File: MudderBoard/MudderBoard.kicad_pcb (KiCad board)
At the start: 2 copper layers, 157 parts, among them K1 AZ2850-2A-12DE, M1 NMOS, M2 NMOS, M3 N-MOSFET, M4 N-MOSFET, Q1 CSD16327Q3, Q2 NPN, U1 LM5122QMH/NOPB, U2 TPS566242DRLR, U3 LP38691DTX-3.3/NOPB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

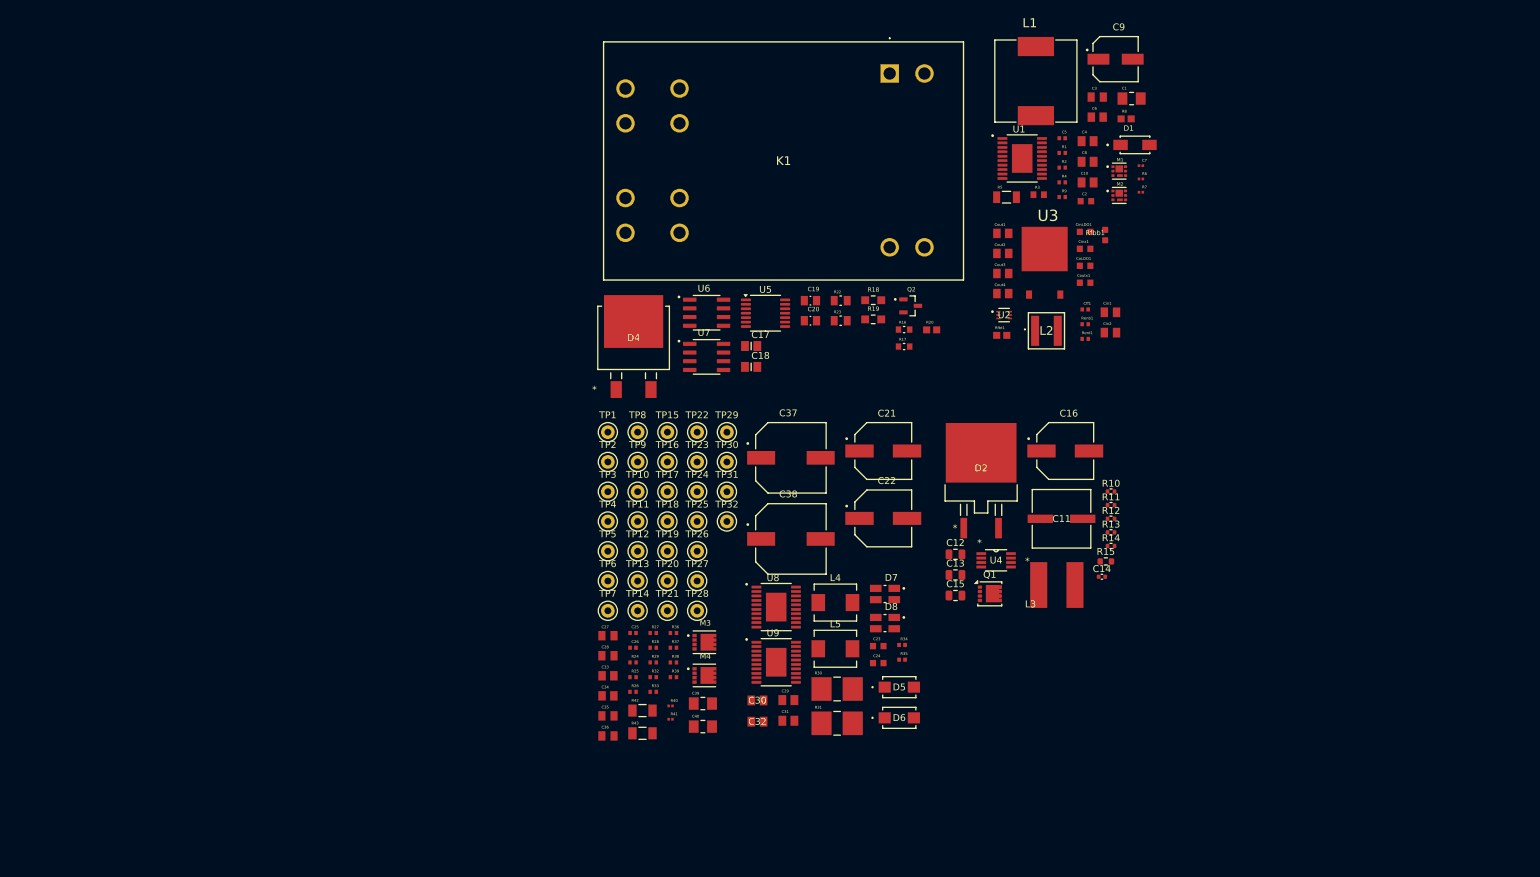
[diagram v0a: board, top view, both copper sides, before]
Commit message: prelim layout for Lidar Boost
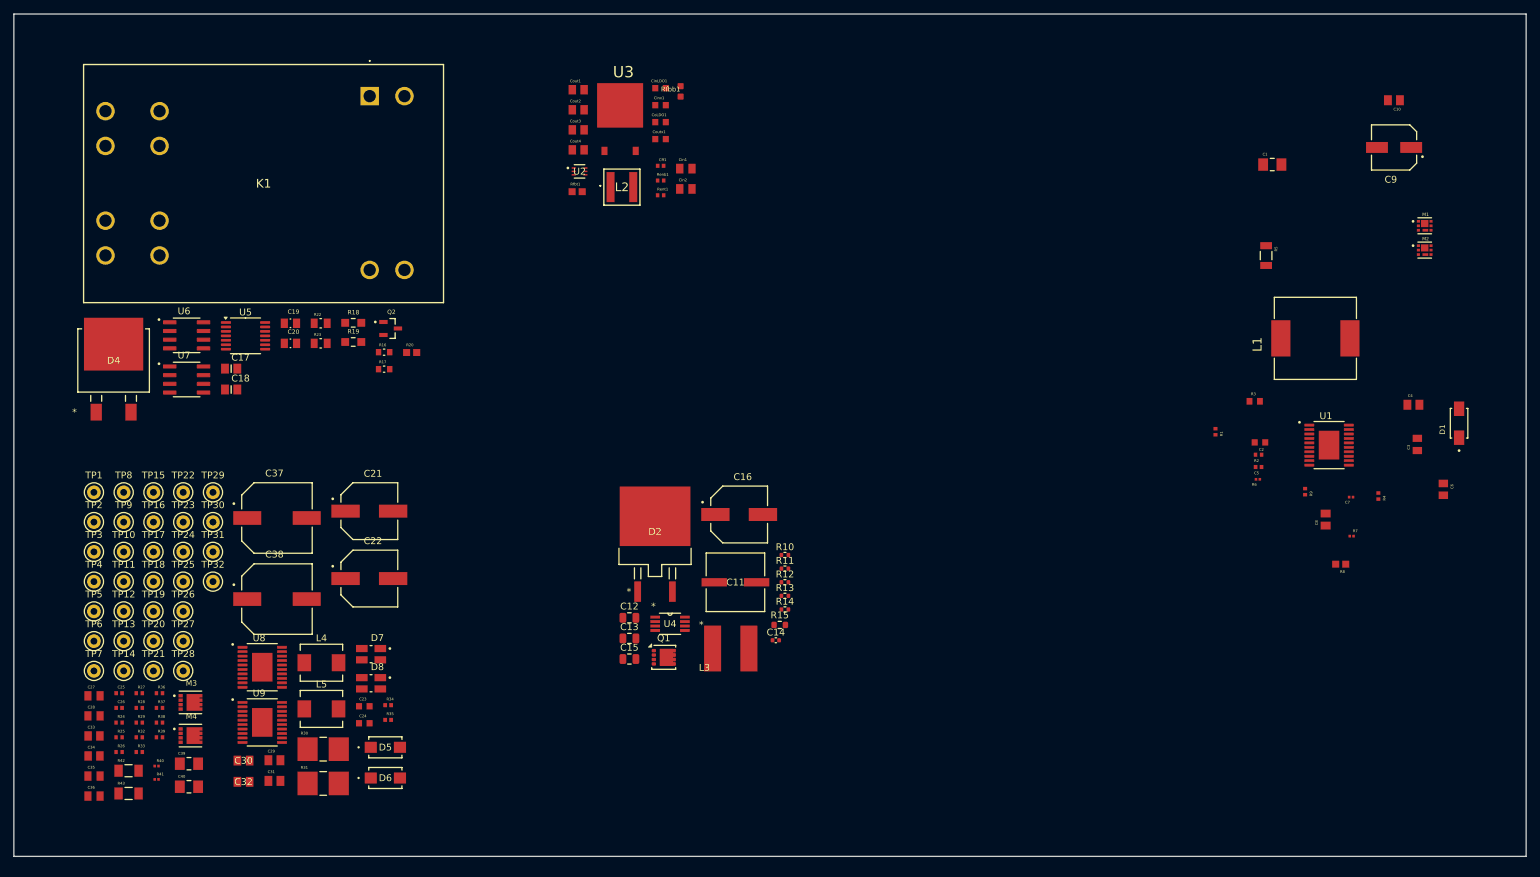
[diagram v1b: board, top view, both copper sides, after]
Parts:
- moved C19 76.1 mm to (56.6, 73.1)
- moved C20 76.1 mm to (56.6, 76.0)
- moved D4 76.1 mm to (30.8, 78.5)
- moved R16 76.1 mm to (70.3, 77.3)
- moved R17 76.1 mm to (70.3, 79.8)
- moved R20 76.1 mm to (74.3, 77.4)
- moved U5 76.1 mm to (50.1, 74.9)
- moved C17 76.1 mm to (48.0, 79.7)
- moved C18 76.1 mm to (48.0, 82.8)
- moved K1 76.1 mm to (68.2, 39.9)
- moved Q2 76.1 mm to (71.3, 73.9)
- moved R18 76.1 mm to (65.8, 73.0)
- moved R19 76.1 mm to (65.8, 75.8)
- moved U6 76.1 mm to (41.5, 74.9)
- moved U7 76.1 mm to (41.5, 81.3)
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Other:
- board outline added: 221 x 123.1 mm

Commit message: Preliminary ESC Boost Layout
Arranged footprints and test points. Still need to route but waiting to see how many layers etc.
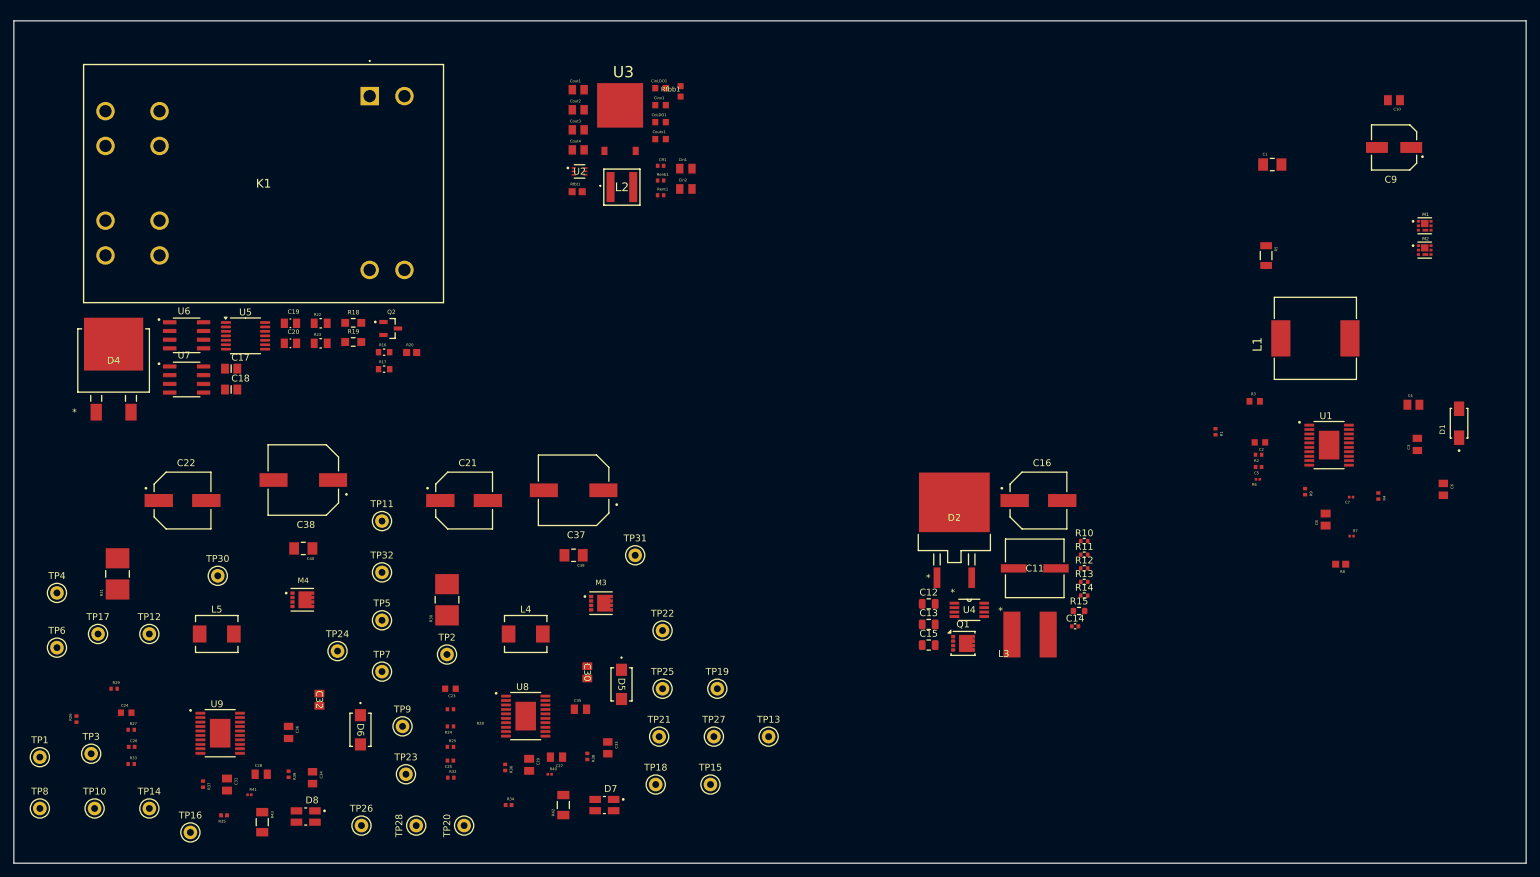
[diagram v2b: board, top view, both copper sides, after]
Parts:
- removed TP29: TestPoint, TestPoint:TestPoint_Keystone_5000-5004_Miniature
- moved TP13 95.3 mm to (126.5, 133.5)
- moved TP15 91.9 mm to (118.0, 140.5)
- moved TP19 83.2 mm to (119.0, 126.5)
- moved TP18 79.2 mm to (110.0, 140.5)
- moved TP27 78.8 mm to (118.5, 133.5)
- moved C33 75.1 mm to (103.0, 135.1), turned to -90 degrees
- moved TP21 74.5 mm to (110.5, 133.5)
- moved TP22 72.9 mm to (111.0, 118.0)
- moved TP25 71.8 mm to (111.0, 126.5)
- moved C35 71.8 mm to (99.0, 129.5)
- moved C27 68.2 mm to (95.5, 136.5), turned to 180 degrees
- moved C39 63.9 mm to (98.0, 107.0), turned to 180 degrees
- moved R42 63.7 mm to (96.5, 143.5), turned to 90 degrees
- moved R38 62.7 mm to (100.0, 136.4), turned to -90 degrees
- moved M3 61.7 mm to (102.0, 114.0)
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
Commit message: PixHawk Layout Updates
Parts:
- added TP29: TestPoint, TestPoint:TestPoint_Keystone_5000-5004_Miniature, F.Cu at (109.1, 81.8)
- added TP33: TestPoint, TestPoint:TestPoint_Pad_D1.0mm, F.Cu at (127.7, 46.7)
- added TP34: TestPoint, TestPoint:TestPoint_Pad_D1.0mm, F.Cu at (119.2, 42.3)
- added TP35: TestPoint, TestPoint:TestPoint_Pad_D1.0mm, F.Cu at (111.7, 61.8)
- added TP36: TestPoint, TestPoint:TestPoint_Pad_D1.0mm, F.Cu at (132.8, 54.8)
- added TP37: TestPoint, TestPoint:TestPoint_Pad_D1.0mm, F.Cu at (128.8, 56.8)
- Rfbb1: value 30K -> 30k
- Rfbt1: value 220K -> 220k
- moved U3 32.7 mm to (129.2, 63.2), turned to 180 degrees
- moved Rfbt1 29.3 mm to (127.8, 51.3), turned to 90 degrees
- moved Cout1 29.0 mm to (120.5, 58.0)
- moved Cout2 28.9 mm to (120.5, 60.8)
- moved Cout3 28.7 mm to (120.5, 63.5)
- moved Cout4 28.6 mm to (120.5, 66.3)
- moved CoLDO1 27.0 mm to (133.9, 57.6), turned to -90 degrees
- moved CinLDO1 23.2 mm to (124.2, 57.6), turned to -90 degrees
- moved U2 21.5 mm to (120.3, 52.3)
- moved Rent1 16.3 mm to (124.3, 45.3), turned to -90 degrees
- moved Rfbb1 15.9 mm to (125.1, 50.3), turned to -90 degrees
- moved Renb1 14.4 mm to (124.3, 47.5), turned to -90 degrees
- moved Coutx1 13.5 mm to (120.5, 55.5)
- moved Cff1 13.3 mm to (123.8, 52.3), turned to 180 degrees
- moved Cinx1 13.2 mm to (120.3, 50.3)
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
